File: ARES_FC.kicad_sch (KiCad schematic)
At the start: 65 parts, among them J1 SWD, J2 TYPE-C-31-M-12, J3 FC_M/P, J4 5V, J5 GND, J6 FC_RF, J7 Conn_01x04_Pin, J8 Conn_01x04_Pin, U1 STM32F401CCU6, U2 AMS1117-3.3, U3 BMP280, U4 BNO055, U5 W25Q32JVSS, U6 PA1616S, Y1 16MHz, Y2 32.768kHz

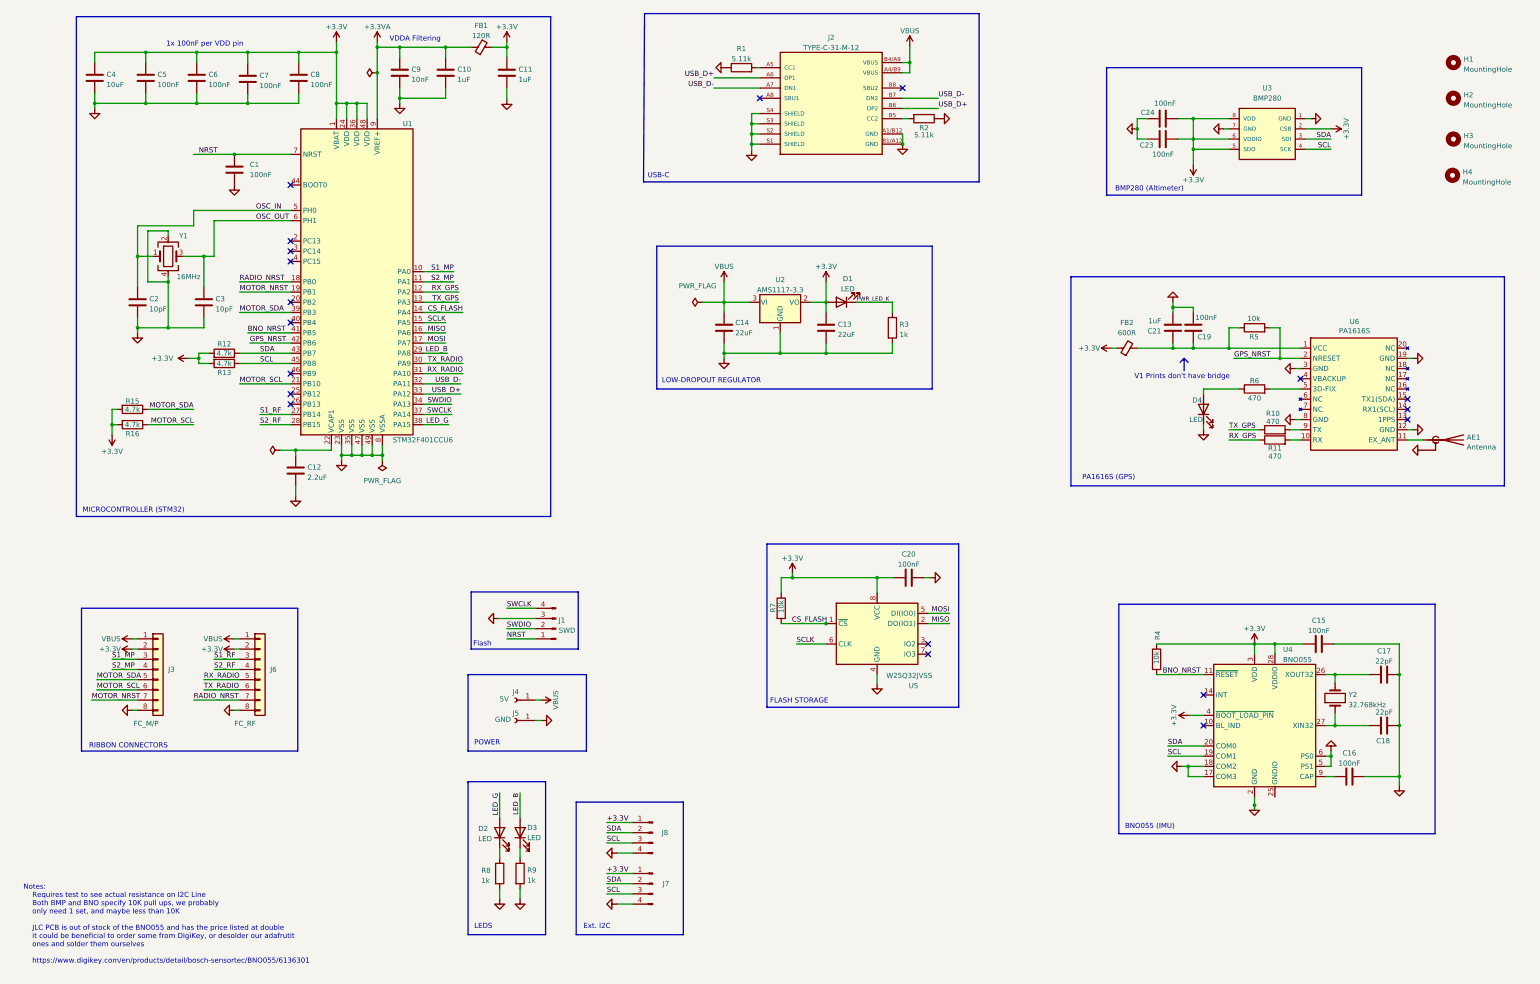
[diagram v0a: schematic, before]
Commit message: cleaned up schematic (aesthetic)
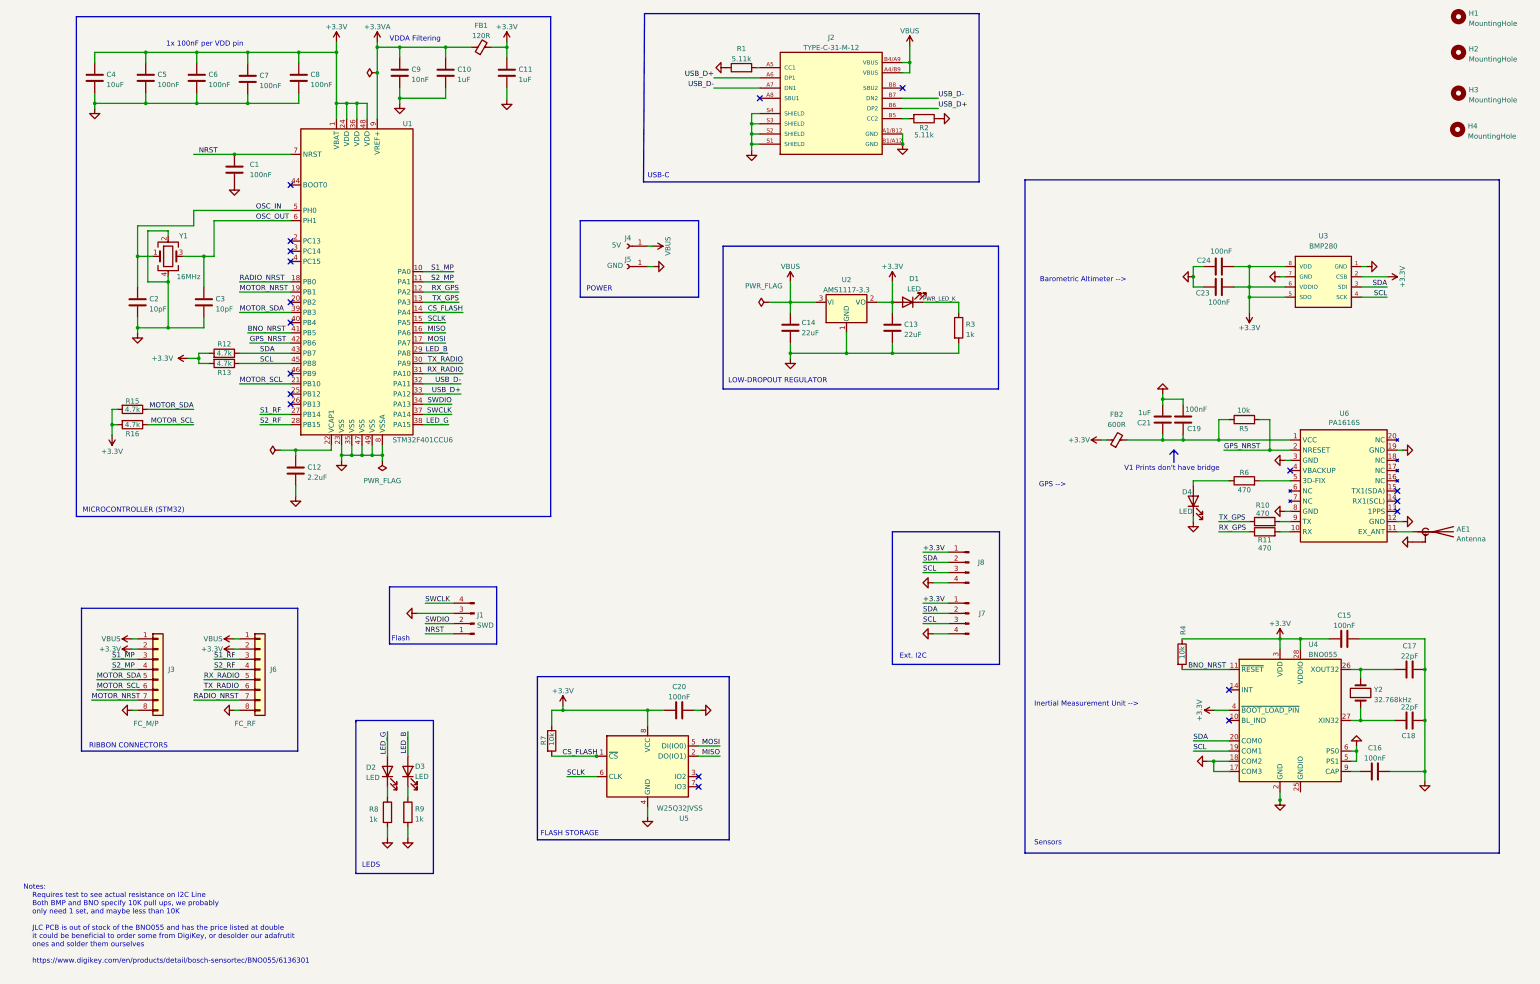
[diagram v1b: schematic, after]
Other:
- note added: "Barometric Altimeter -->"
- note added: "GPS -->"
- note added: "Inertial Measurement Unit -->"
- note added: "Sensors"
- note removed: "BMP280 (Altimeter)"
- note removed: "BNO055 (IMU)"
- note removed: "PA1616S (GPS)"
- moved on the sheet: AE1, C13, C14, C15, C16, C17, C18, C19, C20, C21, C23, C24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

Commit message: added tvs and boot0
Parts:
- added CR1: SMBJ15A, CustomARES:DO-214AASMB_J-BEND_LTF, symbol Custom:SMBJ15A
- added R14: 10k, Resistor_SMD:R_0402_1005Metric, symbol Device:R
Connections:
- net +3.3V: now also CR1.2
- net GND: now also CR1.1, R14.1
- net at U1.44 (BOOT0): now also R14.2
- no-connect marks 19 -> 18
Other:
- note added: "TVS Diode"
- moved on the sheet: C1

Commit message: TVS Diodes at connector lines
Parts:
- removed CR1: SMBJ15A, CustomARES:DO-214AASMB_J-BEND_LTF, symbol Custom:SMBJ15A
- added D10, D11, D12, D13, D14, D15, D16, D17, D18, D19, D20, D21, D22, D23, D5, D6, D7, D8, D9: PESD3V3U1UL, Diode_SMD:D_SOD-882, symbol Diode:PESD3V3U1UL
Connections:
- net GND: now also D10.2 (A), D11.2 (A), D12.2 (A), D13.2 (A), D14.2 (A), D15.2 (A), D16.2 (A), D17.2 (A), D18.2 (A), D19.2 (A), D20.2 (A), D21.2 (A), D22.2 (A), D23.2 (A), D5.2 (A), D6.2 (A), D7.2 (A), D8.2 (A), D9.2 (A)
- net MOTOR_NRST: now also D11.1 (K)
- net MOTOR_SCL: now also D12.1 (K)
- net MOTOR_SDA: now also D13.1 (K)
- net NRST: now also D21.1 (K)
- net RADIO_NRST: now also D20.1 (K)
- net RX_RADIO: now also D18.1 (K)
- net S1_MP: now also D15.1 (K)
- net S1_RF: now also D16.1 (K)
- net S2_MP: now also D14.1 (K)
- net S2_RF: now also D17.1 (K)
- net SCL: now also D10.1 (K), D7.1 (K)
- net SDA: now also D8.1 (K), D9.1 (K)
- net SWCLK: now also D23.1 (K)
- net SWDIO: now also D22.1 (K)
- net TX_RADIO: now also D19.1 (K)
- net USB_D+: now also D5.1 (K)
- net USB_D-: now also D6.1 (K)
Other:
- note removed: "TVS Diode"
- moved on the sheet: C20, D2, D3, J1, J3, J6, J7, J8, R7, R8, R9, U5

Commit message: rerouted BOOT0 pull-down (was on back side)
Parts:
- D10, D11, D12, D13, D14, D15, D16, D17, D18, D19, D20, D21, D22, D23, D5, D6, D7, D8, D9: footprint Diode_SMD:D_SOD-882 -> Diode_SMD:D_0402_1005Metric
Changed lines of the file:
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@@
 			)
 		)
-		(property "Footprint" "Diode_SMD:D_SOD-882"
+		(property "Footprint" "Diode_SMD:D_0402_1005Metric"
 			(at 187.96 137.16 0)
 			(effects
@@
 			)
 		)
-		(property "Footprint" "Diode_SMD:D_SOD-882"
+		(property "Footprint" "Diode_SMD:D_0402_1005Metric"
 			(at 180.34 50.8 0)
 			(effects
@@
 			)
 		)
-		(property "Footprint" "Diode_SMD:D_SOD-882"
+		(property "Footprint" "Diode_SMD:D_0402_1005Metric"
 			(at 36.83 193.04 0)
 			(effects
@@
 			)
 		)
-		(property "Footprint" "Diode_SMD:D_SOD-882"
+		(property "Footprint" "Diode_SMD:D_0402_1005Metric"
 			(at 63.5 193.04 0)
 			(effects
@@
 			)
 		)
-		(property "Datasheet" ""
+		(property "Datasheet" "https://jlcpcb.com/api/file/downloadByFileSystemAccessId/8550723676069908480"
 			(at 220.98 49.53 0)
 			(effects
@@
 			)
 		)
-		(property "Footprint" "Diode_SMD:D_SOD-882"
+		(property "Footprint" "Diode_SMD:D_0402_1005Metric"
 			(at 16.51 193.04 0)
 			(effects
@@
 			)
 		)
-		(property "Footprint" "Diode_SMD:D_SOD-882"
+		(property "Footprint" "Diode_SMD:D_0402_1005Metric"
 			(at 68.58 193.04 0)
 			(effects
@@
 			)
 		)
-		(property "Footprint" "Diode_SMD:D_SOD-882"
+		(property "Footprint" "Diode_SMD:D_0402_1005Metric"
 			(at 187.96 152.4 0)
 			(effects
@@
 			)
 		)
-		(property "Footprint" "Diode_SMD:D_SOD-882"
+		(property "Footprint" "Diode_SMD:D_0402_1005Metric"
 			(at 179.07 152.4 0)
 			(effects
@@
 			)
 		)
-		(property "Footprint" "Diode_SMD:D_SOD-882"
+		(property "Footprint" "Diode_SMD:D_0402_1005Metric"
 			(at 73.66 193.04 0)
 			(effects
@@
 			)
 		)
-		(property "Footprint" "Diode_SMD:D_SOD-882"
+		(property "Footprint" "Diode_SMD:D_0402_1005Metric"
 			(at 132.08 180.34 0)
 			(effects
@@
 			)
 		)
-		(property "Footprint" "Diode_SMD:D_SOD-882"
+		(property "Footprint" "Diode_SMD:D_0402_1005Metric"
 			(at 78.74 193.04 0)
 			(effects
@@
 			)
 		)
-		(property "Footprint" "Diode_SMD:D_SOD-882"
+		(property "Footprint" "Diode_SMD:D_0402_1005Metric"
 			(at 127 180.34 0)
 			(effects
@@
 			)
 		)
-		(property "Footprint" "Diode_SMD:D_SOD-882"
+		(property "Footprint" "Diode_SMD:D_0402_1005Metric"
 			(at 21.59 193.04 0)
 			(effects
@@
 			)
 		)
-		(property "Footprint" "Diode_SMD:D_SOD-882"
+		(property "Footprint" "Diode_SMD:D_0402_1005Metric"
 			(at 187.96 50.8 0)
 			(effects
@@
 			)
 		)
-		(property "Footprint" "Diode_SMD:D_SOD-882"
+		(property "Footprint" "Diode_SMD:D_0402_1005Metric"
 			(at 58.42 193.04 0)
 			(effects
@@
 			)
 		)
-		(property "Footprint" "Diode_SMD:D_SOD-882"
+		(property "Footprint" "Diode_SMD:D_0402_1005Metric"
 			(at 26.67 193.04 0)
 			(effects
@@
 			)
 		)
-		(property "Footprint" "Diode_SMD:D_SOD-882"
+		(property "Footprint" "Diode_SMD:D_0402_1005Metric"
 			(at 31.75 193.04 0)
 			(effects
@@
 			)
 		)
-		(property "Footprint" "Diode_SMD:D_SOD-882"
+		(property "Footprint" "Diode_SMD:D_0402_1005Metric"
 			(at 179.07 137.16 0)
 			(effects
@@
 			)
 		)
-		(property "Footprint" "Diode_SMD:D_SOD-882"
+		(property "Footprint" "Diode_SMD:D_0402_1005Metric"
 			(at 121.92 180.34 0)
 			(effects

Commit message: WINTER 2026 ARES FC ORDER
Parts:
- D10, D11, D12, D13, D14, D15, D16, D17, D18, D19, D20, D21, D22, D23, D5, D6, D7, D8, D9: footprint Diode_SMD:D_0402_1005Metric -> Diode_SMD:D_SOD-882
- R12, R13, R15, R16: LCSC Part C119339 -> C25900
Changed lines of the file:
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@@
 			)
 		)
-		(property "Footprint" "Diode_SMD:D_0402_1005Metric"
+		(property "Footprint" "Diode_SMD:D_SOD-882"
 			(at 187.96 137.16 0)
 			(effects
@@
 			)
 		)
-		(property "Footprint" "Diode_SMD:D_0402_1005Metric"
+		(property "Footprint" "Diode_SMD:D_SOD-882"
 			(at 180.34 50.8 0)
 			(effects
@@
 			)
 		)
-		(property "LCSC Part" "C119339"
+		(property "LCSC Part" "C25900"
 			(at 46.99 125.73 0)
 			(effects
@@
 			)
 		)
-		(property "Footprint" "Diode_SMD:D_0402_1005Metric"
+		(property "Footprint" "Diode_SMD:D_SOD-882"
 			(at 36.83 193.04 0)
 			(effects
@@
 			)
 		)
-		(property "Footprint" "Diode_SMD:D_0402_1005Metric"
+		(property "Footprint" "Diode_SMD:D_SOD-882"
 			(at 63.5 193.04 0)
 			(effects
@@
 			)
 		)
-		(property "LCSC Part" "C119339"
+		(property "LCSC Part" "C25900"
 			(at 69.85 114.3 0)
 			(effects
@@
 			)
 		)
-		(property "Footprint" "Diode_SMD:D_0402_1005Metric"
+		(property "Footprint" "Diode_SMD:D_SOD-882"
 			(at 16.51 193.04 0)
 			(effects
@@
 			)
 		)
-		(property "Footprint" "Diode_SMD:D_0402_1005Metric"
+		(property "Footprint" "Diode_SMD:D_SOD-882"
 			(at 68.58 193.04 0)
 			(effects
@@
 			)
 		)
-		(property "Footprint" "Diode_SMD:D_0402_1005Metric"
+		(property "Footprint" "Diode_SMD:D_SOD-882"
 			(at 187.96 152.4 0)
 			(effects
@@
 			)
 		)
-		(property "Footprint" "Diode_SMD:D_0402_1005Metric"
+		(property "Footprint" "Diode_SMD:D_SOD-882"
 			(at 179.07 152.4 0)
 			(effects
@@
 			)
 		)
-		(property "Footprint" "Diode_SMD:D_0402_1005Metric"
+		(property "Footprint" "Diode_SMD:D_SOD-882"
 			(at 73.66 193.04 0)
 			(effects
@@
 			)
 		)
-		(property "Footprint" "Diode_SMD:D_0402_1005Metric"
+		(property "Footprint" "Diode_SMD:D_SOD-882"
 			(at 132.08 180.34 0)
 			(effects
@@
 			)
 		)
-		(property "Footprint" "Diode_SMD:D_0402_1005Metric"
+		(property "Footprint" "Diode_SMD:D_SOD-882"
 			(at 78.74 193.04 0)
 			(effects
@@
 			)
 		)
-		(property "Footprint" "Diode_SMD:D_0402_1005Metric"
+		(property "Footprint" "Diode_SMD:D_SOD-882"
 			(at 127 180.34 0)
 			(effects
@@
 			)
 		)
-		(property "Footprint" "Diode_SMD:D_0402_1005Metric"
+		(property "Footprint" "Diode_SMD:D_SOD-882"
 			(at 21.59 193.04 0)
 			(effects
@@
 			)
 		)
-		(property "Footprint" "Diode_SMD:D_0402_1005Metric"
+		(property "Footprint" "Diode_SMD:D_SOD-882"
 			(at 187.96 50.8 0)
 			(effects
@@
 			)
 		)
-		(property "LCSC Part" "C119339"
+		(property "LCSC Part" "C25900"
 			(at 46.99 129.54 0)
 			(effects
@@
 			)
 		)
-		(property "Footprint" "Diode_SMD:D_0402_1005Metric"
+		(property "Footprint" "Diode_SMD:D_SOD-882"
 			(at 58.42 193.04 0)
 			(effects
@@
 			)
 		)
-		(property "LCSC Part" "C119339"
+		(property "LCSC Part" "C25900"
 			(at 69.85 111.76 0)
 			(effects
@@
 			)
 		)
-		(property "Footprint" "Diode_SMD:D_0402_1005Metric"
+		(property "Footprint" "Diode_SMD:D_SOD-882"
 			(at 26.67 193.04 0)
 			(effects
@@
 			)
 		)
-		(property "Footprint" "Diode_SMD:D_0402_1005Metric"
+		(property "Footprint" "Diode_SMD:D_SOD-882"
 			(at 31.75 193.04 0)
 			(effects
@@
 			)
 		)
-		(property "Footprint" "Diode_SMD:D_0402_1005Metric"
+		(property "Footprint" "Diode_SMD:D_SOD-882"
 			(at 179.07 137.16 0)
 			(effects
@@
 			)
 		)
-		(property "Footprint" "Diode_SMD:D_0402_1005Metric"
+		(property "Footprint" "Diode_SMD:D_SOD-882"
 			(at 121.92 180.34 0)
 			(effects
